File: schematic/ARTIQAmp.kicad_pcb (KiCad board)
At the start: 8 copper layers, 191 x 152.4 mm, 393 parts, among them IC1 LTC6090CS8E#PBF, IC10 LTC6090CS8E#PBF, IC11 LTC6090CS8E#PBF, IC12 LTC6090CS8E#PBF, IC13 LTC6090CS8E#PBF, IC14 LTC6090CS8E#PBF, IC15 LTC6090CS8E#PBF, IC16 LTC6090CS8E#PBF, IC17 LTC6090CS8E#PBF, IC18 LTC6090CS8E#PBF, IC19 LTC6090CS8E#PBF, IC2 LTC6090CS8E#PBF, IC20 LTC6090CS8E#PBF, IC21 LTC6090CS8E#PBF, IC22 LTC6090CS8E#PBF, IC23 LTC6090CS8E#PBF, IC24 LTC6090CS8E#PBF, IC25 LTC6090CS8E#PBF, IC26 LTC6090CS8E#PBF, IC27 LTC6090CS8E#PBF, IC28 LTC6090CS8E#PBF, IC29 LTC6090CS8E#PBF, IC3 LTC6090CS8E#PBF, IC30 LTC6090CS8E#PBF, IC31 LTC6090CS8E#PBF, IC32 LTC6090CS8E#PBF, IC4 LTC6090CS8E#PBF, IC5 LTC6090CS8E#PBF, IC6 LTC6090CS8E#PBF, IC7 LTC6090CS8E#PBF, IC8 LTC6090CS8E#PBF, IC9 LTC6090CS8E#PBF, J1 Power conneciton, J2 HD68, J3 HD68

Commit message: More layout routing
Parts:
- moved C1 8.35 mm to (111.9, 160.0)
- moved C6 6.91 mm to (121.3, 160.0), turned to 180 degrees
- moved C5 2.77 mm to (121.3, 158.4), turned to 180 degrees
- moved C2 2.53 mm to (111.9, 158.4)
- moved C4 1.31 mm to (119.6, 152.6)
- moved R54 1.13 mm to (144.3, 225.5), turned to 270 degrees
- moved R60 1.13 mm to (161.3, 225.5), turned to 270 degrees
- moved R66 1.13 mm to (178.3, 225.5), turned to 270 degrees
- moved R72 1.13 mm to (195.3, 225.5), turned to 270 degrees
- moved R78 1.13 mm to (212.3, 225.5), turned to 270 degrees
- moved R84 1.13 mm to (229.3, 225.5), turned to 270 degrees
- moved R90 1.13 mm to (246.3, 225.5), turned to 270 degrees
- moved R96 1.13 mm to (127.3, 225.5), turned to 270 degrees
- moved R138 1.13 mm to (258.6, 172.7), turned to 90 degrees
- moved R102 1.13 mm to (156.6, 172.7), turned to 90 degrees
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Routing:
- net (no net): track 0.00 -> 525.3 mm
- net -48V: track 127.1 -> 261.6 mm
- net /D16_IN: track 0.00 -> 127.1 mm
- net /D8_IN: track 0.00 -> 127.0 mm
- net /D16_IN_COM: track 0.00 -> 125.8 mm
- net /D15_IN: track 0.00 -> 110.0 mm
- net /D7_IN: track 0.00 -> 109.8 mm
- net /D15_IN_COM: track 0.00 -> 108.6 mm
- net +48V: track 0.00 -> 99.9 mm, vias 0 -> 32
- net /D14_IN: track 0.00 -> 92.6 mm
- net /D6_IN: track 0.00 -> 92.6 mm
- net /D9_IN_COM: track 0.00 -> 91.9 mm
- net /D14_IN_COM: track 0.00 -> 91.4 mm
- net /D13_IN: track 0.00 -> 75.4 mm
- net /D5_IN: track 0.00 -> 75.4 mm
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- added copper zone on In3.Cu, net +48V
- added copper zone on F.Cu, net /D10_IN_COM
- added copper zone on F.Cu, net /D11_IN_COM
- added copper zone on F.Cu, net /D12_IN_COM
- added copper zone on F.Cu, net /D13_IN_COM
- added copper zone on F.Cu, net /D14_IN_COM
- added copper zone on F.Cu, net /D15_IN_COM
- added copper zone on F.Cu, net /D16_IN_COM
- added copper zone on B.Cu, net /D17_IN_COM
- added copper zone on B.Cu, net /D18_IN_COM
- added copper zone on B.Cu, net /D19_IN_COM
- added copper zone on F.Cu, net /D1_IN_COM
- added copper zone on B.Cu, net /D20_IN_COM
- added copper zone on B.Cu, net /D21_IN_COM
- added copper zone on B.Cu, net /D22_IN_COM
- added copper zone on B.Cu, net /D23_IN_COM
- added copper zone on B.Cu, net /D24_IN_COM
- added copper zone on B.Cu, net /D25_IN_COM
- added copper zone on B.Cu, net /D26_IN_COM
- added copper zone on B.Cu, net /D27_IN_COM
- added copper zone on B.Cu, net /D28_IN_COM
- added copper zone on B.Cu, net /D29_IN_COM
- added copper zone on F.Cu, net /D2_IN_COM
- added copper zone on B.Cu, net /D30_IN_COM
- added copper zone on B.Cu, net /D31_IN_COM
- added copper zone on B.Cu, net /D32_IN_COM
- added copper zone on F.Cu, net /D3_IN_COM
- added copper zone on F.Cu, net /D4_IN_COM
- added copper zone on F.Cu, net /D5_IN_COM
- added copper zone on F.Cu, net /D6_IN_COM
- added copper zone on F.Cu, net /D7_IN_COM
- added copper zone on F.Cu, net /D8_IN_COM
- added copper zone on F.Cu, net /D9_IN_COM
- added copper zone on In1.Cu, net GND
- added copper zone on In6.Cu, net GND

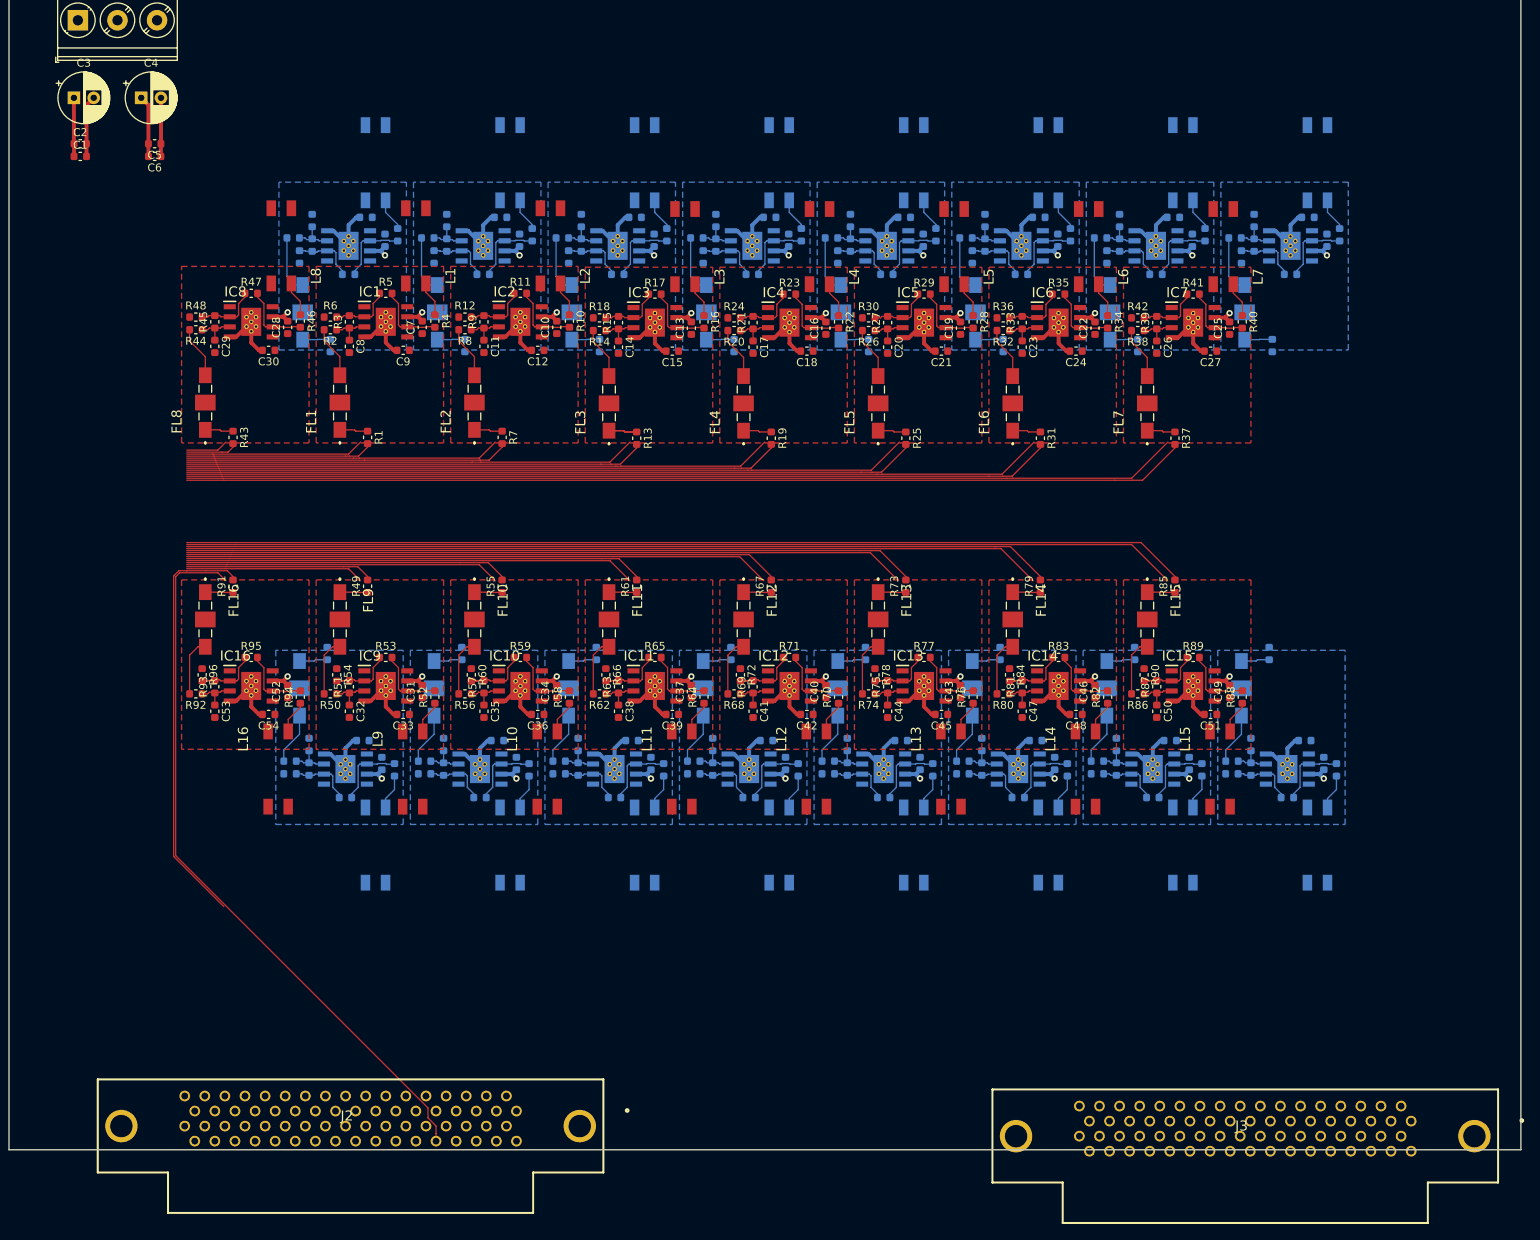
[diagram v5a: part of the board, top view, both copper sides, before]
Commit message: Complete initial layout and swap components around in schematic
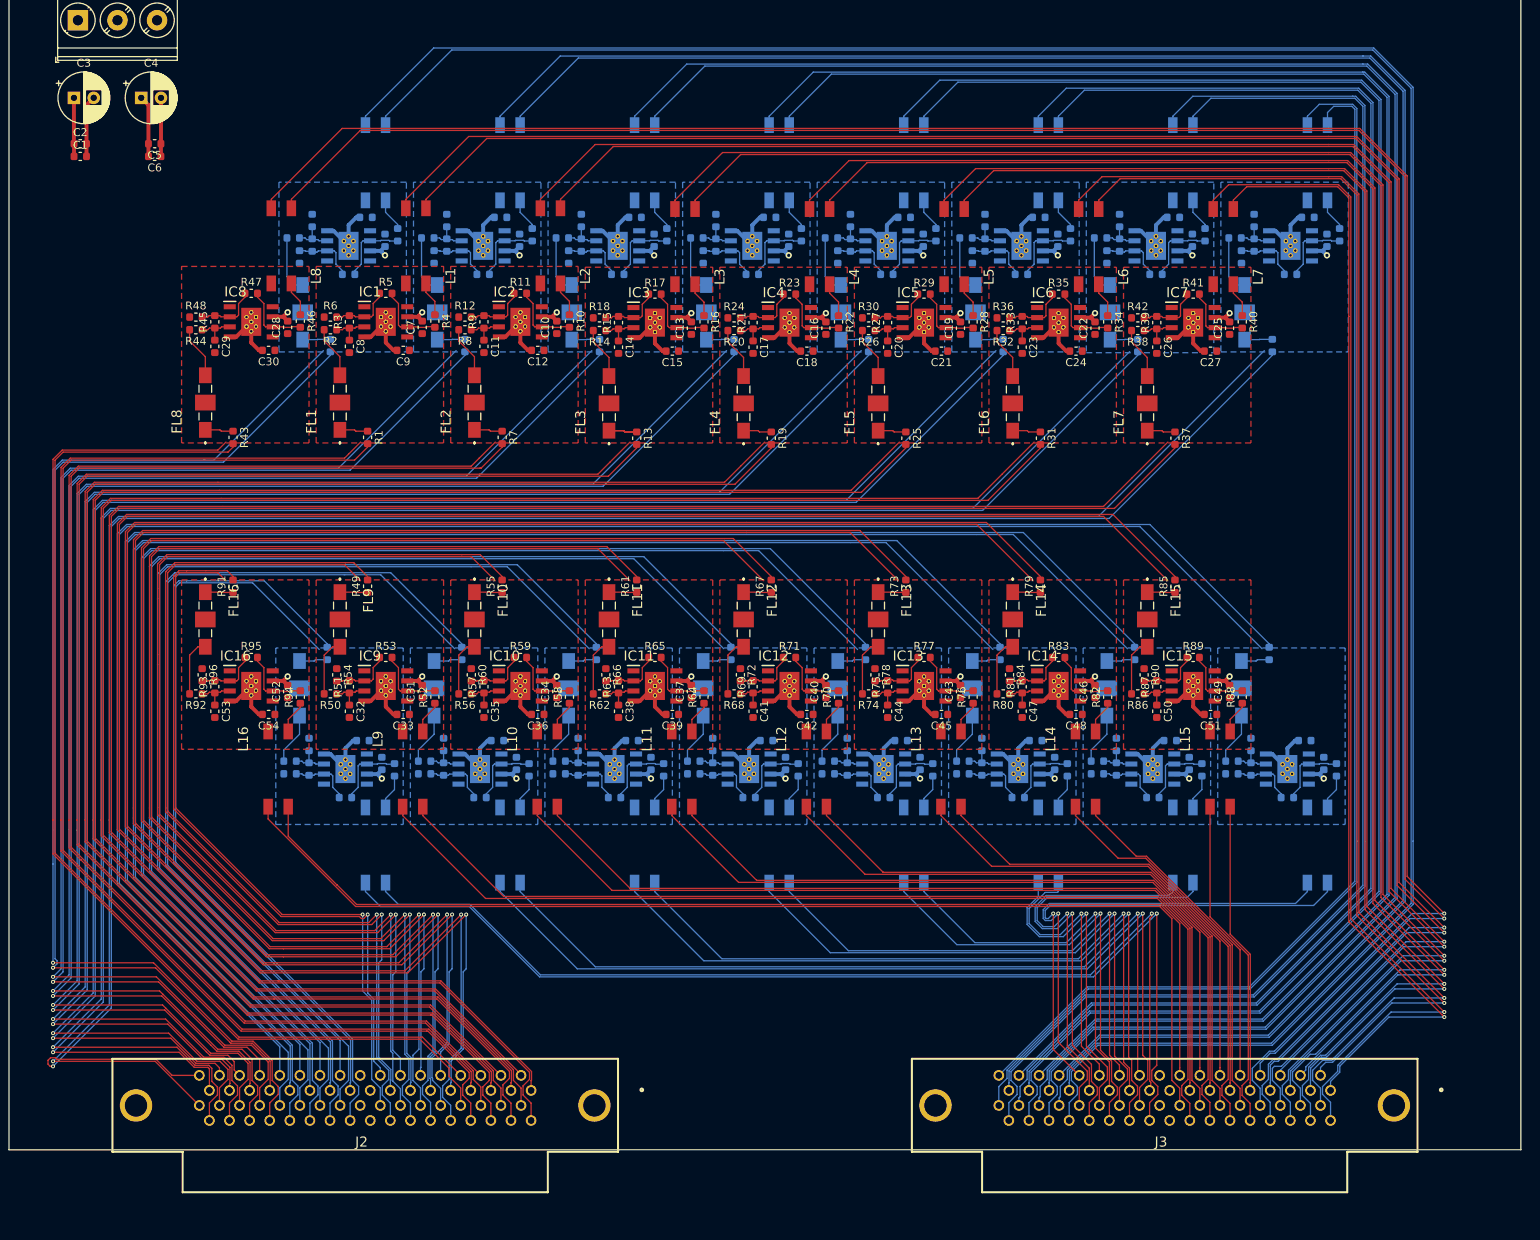
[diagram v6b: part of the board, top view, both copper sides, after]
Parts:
- moved J3 10.4 mm to (248.9, 279.9)
- moved J2 3.78 mm to (147.9, 279.9)
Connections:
- C10 pad 1: /D3_IN_COM -> /D6_IN_COM
- C100 pad 1: /D25_IN_COM -> /D17_IN_COM
- C101 pad 2: /D25_IN_COM -> /D17_IN_COM
- C102 pad 1: /D25_IN_COM -> /D17_IN_COM
- C11 pad 2: /D3_IN_COM -> /D6_IN_COM
- C12 pad 1: /D3_IN_COM -> /D6_IN_COM
- C13 pad 1: /D4_IN_COM -> /D5_IN_COM
- C14 pad 2: /D4_IN_COM -> /D5_IN_COM
- C15 pad 1: /D4_IN_COM -> /D5_IN_COM
- C16 pad 1: /D5_IN_COM -> /D4_IN_COM
- C17 pad 2: /D5_IN_COM -> /D4_IN_COM
- C18 pad 1: /D5_IN_COM -> /D4_IN_COM
- C19 pad 1: /D6_IN_COM -> /D3_IN_COM
- C20 pad 2: /D6_IN_COM -> /D3_IN_COM
- C21 pad 1: /D6_IN_COM -> /D3_IN_COM
- C22 pad 1: /D7_IN_COM -> /D2_IN_COM
- C23 pad 2: /D7_IN_COM -> /D2_IN_COM
- C24 pad 1: /D7_IN_COM -> /D2_IN_COM
- C25 pad 1: /D8_IN_COM -> /D1_IN_COM
- C26 pad 2: /D8_IN_COM -> /D1_IN_COM
- C27 pad 1: /D8_IN_COM -> /D1_IN_COM
- C28 pad 1: /D1_IN_COM -> /D8_IN_COM
- C29 pad 2: /D1_IN_COM -> /D8_IN_COM
- C30 pad 1: /D1_IN_COM -> /D8_IN_COM
- C31 pad 1: /D10_IN_COM -> /D15_IN_COM
- C32 pad 2: /D10_IN_COM -> /D15_IN_COM
- C33 pad 1: /D10_IN_COM -> /D15_IN_COM
- C34 pad 1: /D11_IN_COM -> /D14_IN_COM
- C35 pad 2: /D11_IN_COM -> /D14_IN_COM
- C36 pad 1: /D11_IN_COM -> /D14_IN_COM
- C37 pad 1: /D12_IN_COM -> /D13_IN_COM
- C38 pad 2: /D12_IN_COM -> /D13_IN_COM
- C39 pad 1: /D12_IN_COM -> /D13_IN_COM
- C40 pad 1: /D13_IN_COM -> /D12_IN_COM
- C41 pad 2: /D13_IN_COM -> /D12_IN_COM
- C42 pad 1: /D13_IN_COM -> /D12_IN_COM
- C43 pad 1: /D14_IN_COM -> /D11_IN_COM
- C44 pad 2: /D14_IN_COM -> /D11_IN_COM
- C45 pad 1: /D14_IN_COM -> /D11_IN_COM
- C46 pad 1: /D15_IN_COM -> /D10_IN_COM
- C47 pad 2: /D15_IN_COM -> /D10_IN_COM
- C48 pad 1: /D15_IN_COM -> /D10_IN_COM
- C49 pad 1: /D16_IN_COM -> /D9_IN_COM
- C50 pad 2: /D16_IN_COM -> /D9_IN_COM
- C51 pad 1: /D16_IN_COM -> /D9_IN_COM
- C52 pad 1: /D9_IN_COM -> /D16_IN_COM
- C53 pad 2: /D9_IN_COM -> /D16_IN_COM
- C54 pad 1: /D9_IN_COM -> /D16_IN_COM
- C55 pad 1: /D18_IN_COM -> /D26_IN_COM
- C56 pad 2: /D18_IN_COM -> /D26_IN_COM
- C57 pad 1: /D18_IN_COM -> /D26_IN_COM
- C58 pad 1: /D19_IN_COM -> /D27_IN_COM
- C59 pad 2: /D19_IN_COM -> /D27_IN_COM
- C60 pad 1: /D19_IN_COM -> /D27_IN_COM
- C61 pad 1: /D20_IN_COM -> /D28_IN_COM
- C62 pad 2: /D20_IN_COM -> /D28_IN_COM
- C63 pad 1: /D20_IN_COM -> /D28_IN_COM
- C64 pad 1: /D21_IN_COM -> /D29_IN_COM
- C65 pad 2: /D21_IN_COM -> /D29_IN_COM
- C66 pad 1: /D21_IN_COM -> /D29_IN_COM
- C67 pad 1: /D22_IN_COM -> /D30_IN_COM
- C68 pad 2: /D22_IN_COM -> /D30_IN_COM
- C69 pad 1: /D22_IN_COM -> /D30_IN_COM
- C7 pad 1: /D2_IN_COM -> /D7_IN_COM
- C70 pad 1: /D23_IN_COM -> /D31_IN_COM
- C71 pad 2: /D23_IN_COM -> /D31_IN_COM
- C72 pad 1: /D23_IN_COM -> /D31_IN_COM
- C73 pad 1: /D24_IN_COM -> /D32_IN_COM
- C74 pad 2: /D24_IN_COM -> /D32_IN_COM
- C75 pad 1: /D24_IN_COM -> /D32_IN_COM
- C76 pad 1: /D17_IN_COM -> /D25_IN_COM
- C77 pad 2: /D17_IN_COM -> /D25_IN_COM
- C78 pad 1: /D17_IN_COM -> /D25_IN_COM
- C79 pad 1: /D26_IN_COM -> /D18_IN_COM
- C8 pad 2: /D2_IN_COM -> /D7_IN_COM
- C80 pad 2: /D26_IN_COM -> /D18_IN_COM
- C81 pad 1: /D26_IN_COM -> /D18_IN_COM
- C82 pad 1: /D27_IN_COM -> /D19_IN_COM
- C83 pad 2: /D27_IN_COM -> /D19_IN_COM
- C84 pad 1: /D27_IN_COM -> /D19_IN_COM
- C85 pad 1: /D28_IN_COM -> /D20_IN_COM
- C86 pad 2: /D28_IN_COM -> /D20_IN_COM
- C87 pad 1: /D28_IN_COM -> /D20_IN_COM
- C88 pad 1: /D29_IN_COM -> /D21_IN_COM
- C89 pad 2: /D29_IN_COM -> /D21_IN_COM
- C9 pad 1: /D2_IN_COM -> /D7_IN_COM
- C90 pad 1: /D29_IN_COM -> /D21_IN_COM
- C91 pad 1: /D30_IN_COM -> /D22_IN_COM
- C92 pad 2: /D30_IN_COM -> /D22_IN_COM
- C93 pad 1: /D30_IN_COM -> /D22_IN_COM
- C94 pad 1: /D31_IN_COM -> /D23_IN_COM
- C95 pad 2: /D31_IN_COM -> /D23_IN_COM
- C96 pad 1: /D31_IN_COM -> /D23_IN_COM
- C97 pad 1: /D32_IN_COM -> /D24_IN_COM
- C98 pad 2: /D32_IN_COM -> /D24_IN_COM
- C99 pad 1: /D32_IN_COM -> /D24_IN_COM
- FL1 pad 3: /D2_IN_COM -> /D7_IN_COM
- FL10 pad 3: /D11_IN_COM -> /D14_IN_COM
- FL11 pad 3: /D12_IN_COM -> /D13_IN_COM
- FL12 pad 3: /D13_IN_COM -> /D12_IN_COM
- FL13 pad 3: /D14_IN_COM -> /D11_IN_COM
- FL14 pad 3: /D15_IN_COM -> /D10_IN_COM
- FL15 pad 3: /D16_IN_COM -> /D9_IN_COM
- FL16 pad 3: /D9_IN_COM -> /D16_IN_COM
- FL17 pad 3: /D18_IN_COM -> /D26_IN_COM
- FL18 pad 3: /D19_IN_COM -> /D27_IN_COM
- FL19 pad 3: /D20_IN_COM -> /D28_IN_COM
- FL2 pad 3: /D3_IN_COM -> /D6_IN_COM
- FL20 pad 3: /D21_IN_COM -> /D29_IN_COM
- FL21 pad 3: /D22_IN_COM -> /D30_IN_COM
- FL22 pad 3: /D23_IN_COM -> /D31_IN_COM
- FL23 pad 3: /D24_IN_COM -> /D32_IN_COM
- FL24 pad 3: /D17_IN_COM -> /D25_IN_COM
- FL25 pad 3: /D26_IN_COM -> /D18_IN_COM
- FL26 pad 3: /D27_IN_COM -> /D19_IN_COM
- FL27 pad 3: /D28_IN_COM -> /D20_IN_COM
- FL28 pad 3: /D29_IN_COM -> /D21_IN_COM
- FL29 pad 3: /D30_IN_COM -> /D22_IN_COM
- FL3 pad 3: /D4_IN_COM -> /D5_IN_COM
- FL30 pad 3: /D31_IN_COM -> /D23_IN_COM
- FL31 pad 3: /D32_IN_COM -> /D24_IN_COM
- FL32 pad 3: /D25_IN_COM -> /D17_IN_COM
- FL4 pad 3: /D5_IN_COM -> /D4_IN_COM
- FL5 pad 3: /D6_IN_COM -> /D3_IN_COM
- FL6 pad 3: /D7_IN_COM -> /D2_IN_COM
- FL7 pad 3: /D8_IN_COM -> /D1_IN_COM
- FL8 pad 3: /D1_IN_COM -> /D8_IN_COM
- FL9 pad 3: /D10_IN_COM -> /D15_IN_COM
- L1 pad 1: /D2_IN_COM -> /D7_IN_COM
- L1 pad 3: /D2_HV_OUT -> /D7_HV_OUT
- L1 pad 4: /D2_HV_OUT_COM -> /D7_HV_OUT_COM
- L10 pad 2: /D11_IN_COM -> /D14_IN_COM
- L10 pad 3: /D11_HV_OUT_COM -> /D14_HV_OUT_COM
- L10 pad 4: /D11_HV_OUT -> /D14_HV_OUT
- L11 pad 2: /D12_IN_COM -> /D13_IN_COM
- L11 pad 3: /D12_HV_OUT_COM -> /D13_HV_OUT_COM
- L11 pad 4: /D12_HV_OUT -> /D13_HV_OUT
- L12 pad 2: /D13_IN_COM -> /D12_IN_COM
- L12 pad 3: /D13_HV_OUT_COM -> /D12_HV_OUT_COM
- L12 pad 4: /D13_HV_OUT -> /D12_HV_OUT
- L13 pad 2: /D14_IN_COM -> /D11_IN_COM
- L13 pad 3: /D14_HV_OUT_COM -> /D11_HV_OUT_COM
- L13 pad 4: /D14_HV_OUT -> /D11_HV_OUT
- L14 pad 2: /D15_IN_COM -> /D10_IN_COM
- L14 pad 3: /D15_HV_OUT_COM -> /D10_HV_OUT_COM
- L14 pad 4: /D15_HV_OUT -> /D10_HV_OUT
- L15 pad 2: /D16_IN_COM -> /D9_IN_COM
- L15 pad 3: /D16_HV_OUT_COM -> /D9_HV_OUT_COM
- L15 pad 4: /D16_HV_OUT -> /D9_HV_OUT
- L16 pad 2: /D9_IN_COM -> /D16_IN_COM
- L16 pad 3: /D9_HV_OUT_COM -> /D16_HV_OUT_COM
- L16 pad 4: /D9_HV_OUT -> /D16_HV_OUT
- L17 pad 2: /D18_IN_COM -> /D26_IN_COM
- L17 pad 3: /D18_HV_OUT_COM -> /D26_HV_OUT_COM
- L17 pad 4: /D18_HV_OUT -> /D26_HV_OUT
- L18 pad 2: /D19_IN_COM -> /D27_IN_COM
- L18 pad 3: /D19_HV_OUT_COM -> /D27_HV_OUT_COM
- L18 pad 4: /D19_HV_OUT -> /D27_HV_OUT
- L19 pad 2: /D20_IN_COM -> /D28_IN_COM
- L19 pad 3: /D20_HV_OUT_COM -> /D28_HV_OUT_COM
- L19 pad 4: /D20_HV_OUT -> /D28_HV_OUT
- L2 pad 1: /D3_IN_COM -> /D6_IN_COM
- L2 pad 3: /D3_HV_OUT -> /D6_HV_OUT
- L2 pad 4: /D3_HV_OUT_COM -> /D6_HV_OUT_COM
- L20 pad 2: /D21_IN_COM -> /D29_IN_COM
- L20 pad 3: /D21_HV_OUT_COM -> /D29_HV_OUT_COM
- L20 pad 4: /D21_HV_OUT -> /D29_HV_OUT
- L21 pad 2: /D22_IN_COM -> /D30_IN_COM
- L21 pad 3: /D22_HV_OUT_COM -> /D30_HV_OUT_COM
- L21 pad 4: /D22_HV_OUT -> /D30_HV_OUT
- L22 pad 2: /D23_IN_COM -> /D31_IN_COM
- L22 pad 3: /D23_HV_OUT_COM -> /D31_HV_OUT_COM
- L22 pad 4: /D23_HV_OUT -> /D31_HV_OUT
- L23 pad 2: /D24_IN_COM -> /D32_IN_COM
- L23 pad 3: /D24_HV_OUT_COM -> /D32_HV_OUT_COM
- L23 pad 4: /D24_HV_OUT -> /D32_HV_OUT
- L24 pad 2: /D17_IN_COM -> /D25_IN_COM
- L24 pad 3: /D17_HV_OUT_COM -> /D25_HV_OUT_COM
- L24 pad 4: /D17_HV_OUT -> /D25_HV_OUT
- L25 pad 1: /D26_IN_COM -> /D18_IN_COM
- L25 pad 3: /D26_HV_OUT -> /D18_HV_OUT
- L25 pad 4: /D26_HV_OUT_COM -> /D18_HV_OUT_COM
- L26 pad 1: /D27_IN_COM -> /D19_IN_COM
- L26 pad 3: /D27_HV_OUT -> /D19_HV_OUT
- L26 pad 4: /D27_HV_OUT_COM -> /D19_HV_OUT_COM
- L27 pad 1: /D28_IN_COM -> /D20_IN_COM
- L27 pad 3: /D28_HV_OUT -> /D20_HV_OUT
- L27 pad 4: /D28_HV_OUT_COM -> /D20_HV_OUT_COM
- L28 pad 1: /D29_IN_COM -> /D21_IN_COM
- L28 pad 3: /D29_HV_OUT -> /D21_HV_OUT
- L28 pad 4: /D29_HV_OUT_COM -> /D21_HV_OUT_COM
- L29 pad 1: /D30_IN_COM -> /D22_IN_COM
- L29 pad 3: /D30_HV_OUT -> /D22_HV_OUT
- L29 pad 4: /D30_HV_OUT_COM -> /D22_HV_OUT_COM
- L3 pad 1: /D4_IN_COM -> /D5_IN_COM
- L3 pad 3: /D4_HV_OUT -> /D5_HV_OUT
- L3 pad 4: /D4_HV_OUT_COM -> /D5_HV_OUT_COM
- L30 pad 1: /D31_IN_COM -> /D23_IN_COM
- L30 pad 3: /D31_HV_OUT -> /D23_HV_OUT
- L30 pad 4: /D31_HV_OUT_COM -> /D23_HV_OUT_COM
- L31 pad 1: /D32_IN_COM -> /D24_IN_COM
- L31 pad 3: /D32_HV_OUT -> /D24_HV_OUT
- L31 pad 4: /D32_HV_OUT_COM -> /D24_HV_OUT_COM
- L32 pad 1: /D25_IN_COM -> /D17_IN_COM
- L32 pad 3: /D25_HV_OUT -> /D17_HV_OUT
- L32 pad 4: /D25_HV_OUT_COM -> /D17_HV_OUT_COM
- L4 pad 1: /D5_IN_COM -> /D4_IN_COM
- L4 pad 3: /D5_HV_OUT -> /D4_HV_OUT
- L4 pad 4: /D5_HV_OUT_COM -> /D4_HV_OUT_COM
- L5 pad 1: /D6_IN_COM -> /D3_IN_COM
- L5 pad 3: /D6_HV_OUT -> /D3_HV_OUT
- L5 pad 4: /D6_HV_OUT_COM -> /D3_HV_OUT_COM
- L6 pad 1: /D7_IN_COM -> /D2_IN_COM
- L6 pad 3: /D7_HV_OUT -> /D2_HV_OUT
- L6 pad 4: /D7_HV_OUT_COM -> /D2_HV_OUT_COM
- L7 pad 1: /D8_IN_COM -> /D1_IN_COM
- L7 pad 3: /D8_HV_OUT -> /D1_HV_OUT
- L7 pad 4: /D8_HV_OUT_COM -> /D1_HV_OUT_COM
- L8 pad 1: /D1_IN_COM -> /D8_IN_COM
- L8 pad 3: /D1_HV_OUT -> /D8_HV_OUT
- L8 pad 4: /D1_HV_OUT_COM -> /D8_HV_OUT_COM
- L9 pad 2: /D10_IN_COM -> /D15_IN_COM
- L9 pad 3: /D10_HV_OUT_COM -> /D15_HV_OUT_COM
- L9 pad 4: /D10_HV_OUT -> /D15_HV_OUT
- R1 pad 2: /D2_IN -> /D7_IN
- R102 pad 1: /D18_IN_COM -> /D26_IN_COM
- R103 pad 2: /D19_IN -> /D27_IN
- R108 pad 1: /D19_IN_COM -> /D27_IN_COM
- R109 pad 2: /D20_IN -> /D28_IN
- R114 pad 1: /D20_IN_COM -> /D28_IN_COM
- R115 pad 2: /D21_IN -> /D29_IN
- R12 pad 1: /D3_IN_COM -> /D6_IN_COM
- R120 pad 1: /D21_IN_COM -> /D29_IN_COM
- R121 pad 2: /D22_IN -> /D30_IN
- R126 pad 1: /D22_IN_COM -> /D30_IN_COM
- R127 pad 2: /D23_IN -> /D31_IN
- R13 pad 2: /D4_IN -> /D5_IN
- R132 pad 1: /D23_IN_COM -> /D31_IN_COM
- R133 pad 2: /D24_IN -> /D32_IN
- R138 pad 1: /D24_IN_COM -> /D32_IN_COM
- R139 pad 2: /D17_IN -> /D25_IN
- R144 pad 1: /D17_IN_COM -> /D25_IN_COM
- R145 pad 2: /D26_IN -> /D18_IN
- R150 pad 1: /D26_IN_COM -> /D18_IN_COM
- R151 pad 2: /D27_IN -> /D19_IN
- R156 pad 1: /D27_IN_COM -> /D19_IN_COM
- R157 pad 2: /D28_IN -> /D20_IN
- R162 pad 1: /D28_IN_COM -> /D20_IN_COM
- R163 pad 2: /D29_IN -> /D21_IN
- R168 pad 1: /D29_IN_COM -> /D21_IN_COM
- R169 pad 2: /D30_IN -> /D22_IN
- R174 pad 1: /D30_IN_COM -> /D22_IN_COM
- R175 pad 2: /D31_IN -> /D23_IN
- R18 pad 1: /D4_IN_COM -> /D5_IN_COM
- R180 pad 1: /D31_IN_COM -> /D23_IN_COM
- R181 pad 2: /D32_IN -> /D24_IN
- R186 pad 1: /D32_IN_COM -> /D24_IN_COM
- R187 pad 2: /D25_IN -> /D17_IN
- R19 pad 2: /D5_IN -> /D4_IN
- R192 pad 1: /D25_IN_COM -> /D17_IN_COM
- R24 pad 1: /D5_IN_COM -> /D4_IN_COM
- R25 pad 2: /D6_IN -> /D3_IN
- R30 pad 1: /D6_IN_COM -> /D3_IN_COM
- R31 pad 2: /D7_IN -> /D2_IN
- R36 pad 1: /D7_IN_COM -> /D2_IN_COM
- R37 pad 2: /D8_IN -> /D1_IN
- R42 pad 1: /D8_IN_COM -> /D1_IN_COM
- R43 pad 2: /D1_IN -> /D8_IN
- R48 pad 1: /D1_IN_COM -> /D8_IN_COM
- R49 pad 2: /D10_IN -> /D15_IN
- R54 pad 1: /D10_IN_COM -> /D15_IN_COM
- R55 pad 2: /D11_IN -> /D14_IN
- R6 pad 1: /D2_IN_COM -> /D7_IN_COM
- R60 pad 1: /D11_IN_COM -> /D14_IN_COM
- R61 pad 2: /D12_IN -> /D13_IN
- R66 pad 1: /D12_IN_COM -> /D13_IN_COM
- R67 pad 2: /D13_IN -> /D12_IN
- R7 pad 2: /D3_IN -> /D6_IN
- R72 pad 1: /D13_IN_COM -> /D12_IN_COM
- R73 pad 2: /D14_IN -> /D11_IN
- R78 pad 1: /D14_IN_COM -> /D11_IN_COM
- R79 pad 2: /D15_IN -> /D10_IN
- R84 pad 1: /D15_IN_COM -> /D10_IN_COM
- R85 pad 2: /D16_IN -> /D9_IN
- R90 pad 1: /D16_IN_COM -> /D9_IN_COM
- R91 pad 2: /D9_IN -> /D16_IN
- R96 pad 1: /D9_IN_COM -> /D16_IN_COM
- R97 pad 2: /D18_IN -> /D26_IN
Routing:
- net (no net): track 525.3 -> 0.00 mm
- net /D25_HV_OUT_COM: track 0.00 -> 301.2 mm
- net /D25_HV_OUT: track 0.00 -> 293.6 mm
- net /D8_HV_OUT_COM: track 0.00 -> 283.4 mm, vias 0 -> 1
- net /D26_HV_OUT_COM: track 0.00 -> 279.3 mm
- net /D8_HV_OUT: track 0.00 -> 276.0 mm, vias 0 -> 1
- net /D26_HV_OUT: track 0.00 -> 272.3 mm
- net /D7_HV_OUT_COM: track 0.00 -> 266.3 mm, vias 0 -> 1
- net /D27_HV_OUT_COM: track 0.00 -> 263.1 mm
- net /D7_HV_OUT: track 0.00 -> 258.9 mm, vias 0 -> 1
- net /D27_HV_OUT: track 0.00 -> 255.5 mm
- net /D1_IN_COM: track 0.00 -> 250.1 mm
- net /D32_IN: track 0.00 -> 248.7 mm, vias 0 -> 1
- net /D32_IN_COM: track 0.00 -> 246.5 mm, vias 0 -> 1
- net /D6_HV_OUT_COM: track 0.00 -> 245.6 mm, vias 0 -> 1
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
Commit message: Saftey commit while removing internal layers
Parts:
- moved C55 1.00 mm to (167.4, 171.6)
- moved C56 1.00 mm to (158.2, 169.1)
- moved C57 1.00 mm to (165.0, 168.7)
- moved C58 1.00 mm to (184.4, 171.6)
- moved C59 1.00 mm to (175.2, 169.1)
- moved C60 1.00 mm to (182.0, 168.7)
- moved C61 1.00 mm to (201.4, 171.6)
- moved C62 1.00 mm to (192.2, 169.1)
- moved C63 1.00 mm to (199.0, 168.7)
- moved C64 1.00 mm to (218.4, 171.6)
- moved C65 1.00 mm to (209.2, 169.1)
- moved C66 1.00 mm to (216.0, 168.7)
- moved C67 1.00 mm to (235.4, 171.6)
- moved C68 1.00 mm to (226.2, 169.1)
- moved C69 1.00 mm to (233.0, 168.7)
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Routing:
- net /D17_IN_COM: track 99.3 -> 101.6 mm
- net /D21_IN_COM: track 176.3 -> 178.5 mm
- net /D21_IN: track 173.5 -> 175.7 mm
- net /D20_IN: track 152.2 -> 154.4 mm
- net /D18_IN: track 113.6 -> 115.7 mm
- net /D23_IN: track 212.2 -> 214.4 mm
- net /D19_IN: track 134.8 -> 137.0 mm
- net /D17_IN: track 96.4 -> 98.6 mm
- net /D24_IN: track 229.6 -> 231.8 mm
- net /D22_IN: track 191.0 -> 193.2 mm
- net /D23_IN_COM: track 215.1 -> 217.3 mm
- net /D19_IN_COM: track 137.7 -> 139.8 mm
- net /D24_IN_COM: track 232.6 -> 234.7 mm
- net /D20_IN_COM: track 155.2 -> 157.3 mm
- net /D18_IN_COM: track 116.5 -> 118.6 mm
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- added copper zone on In2.Cu, net +48V
- added copper zone on In3.Cu, net -48V
- added copper zone on F.Cu, net GND
- added copper zone on In4.Cu, net GND
- removed copper zone on In3.Cu, net +48V
- removed copper zone on In4.Cu, net -48V
- removed copper zone on In6.Cu, net GND
